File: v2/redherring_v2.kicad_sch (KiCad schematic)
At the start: 182 parts, among them J4 Pimaroni Trackball, Q2 TIP120, SW1 SW_PUSH_LED, SW10 SW_PUSH_LED, SW11 SW_PUSH_LED, SW12 SW_PUSH_LED, SW13 SW_PUSH_LED, SW14 SW_PUSH_LED, SW15 SW_PUSH_LED, SW16 SW_PUSH_LED, SW17 SW_PUSH_LED, SW18 SW_PUSH_LED, SW19 SW_PUSH_LED, SW2 SW_PUSH_LED, SW20 SW_PUSH_LED, SW21 SW_PUSH_LED, SW22 SW_PUSH_LED, SW23 SW_PUSH_LED, SW24 SW_PUSH_LED, SW25 SW_PUSH_LED, SW26 SW_PUSH_LED, SW27 SW_PUSH_LED, SW28 SW_PUSH_LED, SW29 SW_PUSH_LED, SW3 SW_PUSH_LED, SW30 SW_PUSH_LED, SW31 SW_PUSH_LED, SW32 SW_PUSH_LED, SW33 SW_PUSH_LED, SW34 SW_PUSH_LED, SW35 SW_PUSH_LED, SW36 SW_PUSH_LED, SW37 SW_PUSH_LED, SW38 SW_PUSH_LED, SW39 SW_PUSH_LED, SW4 SW_PUSH_LED, SW40 SW_PUSH_LED, SW41 SW_PUSH_LED, SW42 SW_PUSH_LED, SW43 SW_PUSH_LED, SW44 SW_PUSH_LED, SW45 SW_PUSH_LED, SW46 SW_PUSH_LED, SW47 SW_PUSH_LED, SW48 SW_PUSH_LED, SW49 SW_PUSH_LED, SW5 SW_PUSH_LED, SW50 SW_PUSH_LED, SW51 SW_PUSH_LED, SW52 SW_PUSH_LED, SW53 SW_PUSH_LED, SW54 SW_PUSH_LED, SW55 SW_PUSH_LED, SW56 SW_PUSH_LED, SW57 SW_PUSH_LED, SW58 SW_PUSH_LED, SW59 SW_PUSH_LED, SW6 SW_PUSH_LED, SW60 SW_PUSH_LED, SW61 SW_PUSH_LED, SW62 SW_PUSH_LED, SW63 SW_PUSH_LED, SW64 SW_PUSH_LED, SW65 SW_PUSH_LED, SW66 SW_PUSH_LED, SW67 SW_PUSH_LED, SW68 SW_PUSH_LED, SW69 SW_PUSH_LED, SW7 SW_PUSH_LED, SW71 SW_PUSH_LED, SW72 SW_PUSH_LED, SW73 SW_PUSH_LED, SW74 SW_PUSH_LED, SW75 SW_PUSH_LED, SW76 SW_PUSH_LED, SW77 SW_PUSH_LED, SW78 SW_PUSH_LED, SW79 SW_PUSH_LED, SW8 SW_PUSH_LED, SW81 SW_PUSH_LED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

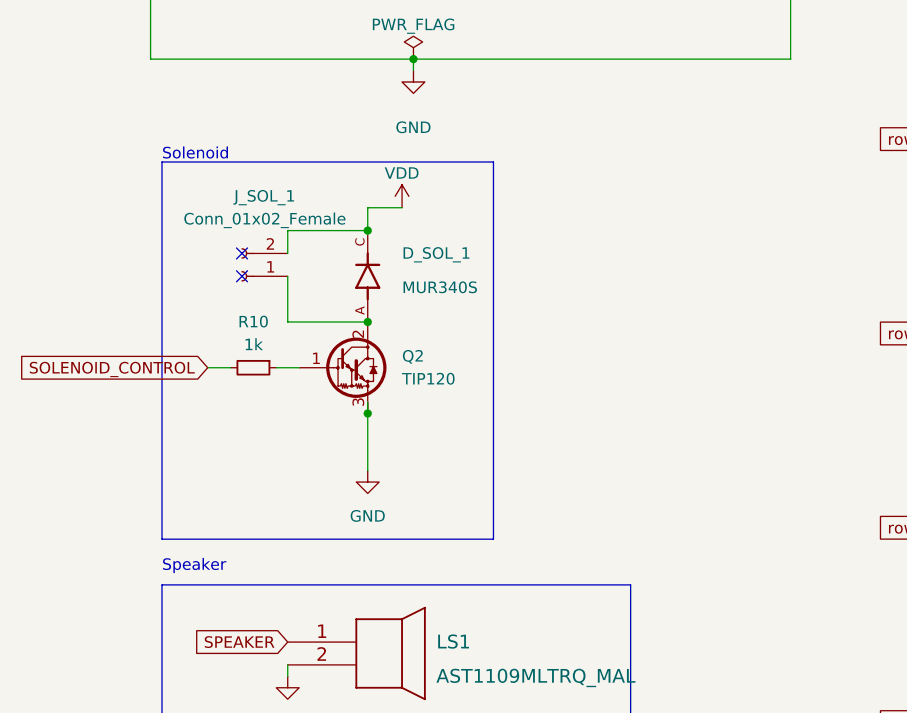
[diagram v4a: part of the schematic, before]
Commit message: Added 3d models
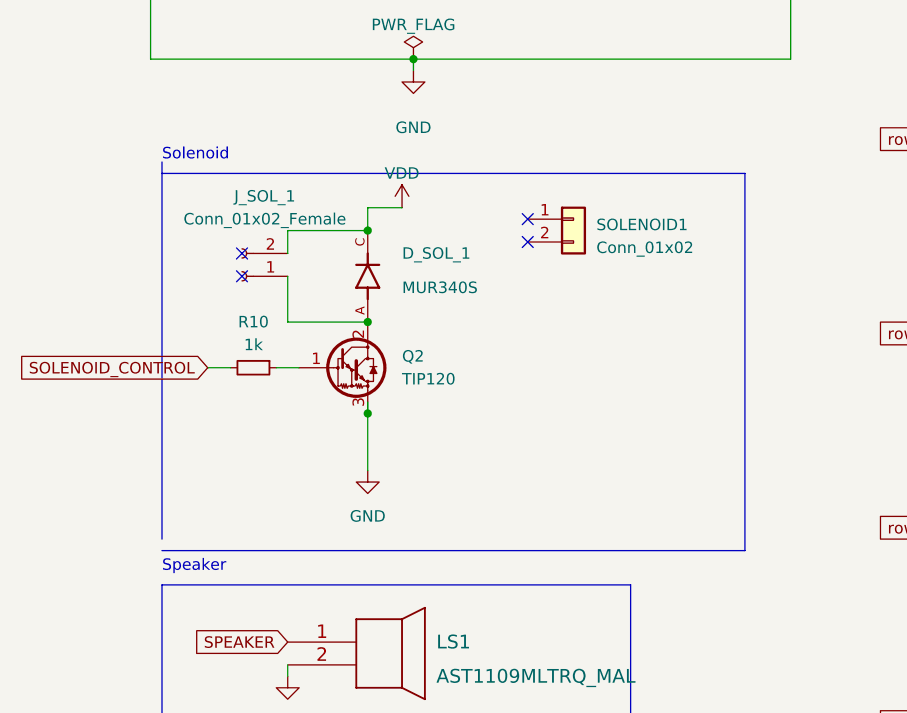
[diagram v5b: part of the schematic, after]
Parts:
- added SOLENOID1: Conn_01x02, red_herring_v2_footprints:uxcell a14092600ux0438 solenoid, symbol Connector_Generic:Conn_01x02
- LS1: footprint ergodonk_kicad_library:AST1109MLTRQ CANTOR MX -> red_herring_v2_footprints:AST1109MLTRQ CANTOR MX
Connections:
- no-connect marks 11 -> 13
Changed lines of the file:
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@@
   (junction (at 248.92 149.86) (diameter 0) (color 0 0 0 0)
   )
+  (no_connect (at 58.42 101.6))
   (no_connect (at 26.67 107.95))
   (no_connect (at 48.26 76.2))
@@
   (no_connect (at 63.5 33.02))
   (no_connect (at 63.5 30.48))
+  (no_connect (at 58.42 104.14))
   (wire (pts (xy 130.81 200.66) (xy 149.86 200.66))
     (stroke (width 0) (type default))
@@
     (stroke (width 0) (type default))
   )
-  (polyline (pts (xy 17.78 95.25) (xy 54.61 95.25))
+  (polyline (pts (xy 17.78 96.52) (xy 82.55 96.52))
     (stroke (width 0) (type default))
   )
@@
     (stroke (width 0) (type default))
   )
-  (polyline (pts (xy 17.78 137.16) (xy 54.61 137.16))
+  (polyline (pts (xy 17.78 138.43) (xy 82.55 138.43))
     (stroke (width 0) (type default))
   )
@@
     (stroke (width 0) (type default))
   )
-  (polyline (pts (xy 54.61 137.16) (xy 54.61 95.25))
+  (polyline (pts (xy 82.55 138.43) (xy 82.55 96.52))
     (stroke (width 0) (type default))
   )
@@
     )
   )
+  (symbol (lib_id "Connector_Generic:Conn_01x02") (at 63.5 101.6 0) (unit 1)
+    (in_bom yes) (on_board yes) (dnp no) (fields_autoplaced)
+    (property "Reference" "SOLENOID1" (at 66.04 102.235 0)
+      (effects (font (size 1.27 1.27)) (justify left))
+    )
+    (property "Value" "Conn_01x02" (at 66.04 104.775 0)
+      (effects (font (size 1.27 1.27)) (justify left))
+    )
+    (property "Footprint" "red_herring_v2_footprints:uxcell a14092600ux0438 solenoid" (at 63.5 101.6 0)
+      (effects (font (size 1.27 1.27)) hide)
+    )
+    (property "Datasheet" "~" (at 63.5 101.6 0)
+      (effects (font (size 1.27 1.27)) hide)
+    )
+    (pin "1")
+    (pin "2")
+    (instances
+      (project "redherring_v2"
+        (path "/ac76b486-7d71-4fdd-84d6-1ecd5326b6c6"
+          (reference "SOLENOID1") (unit 1)
+        )
+      )
+    )
+  )
   (symbol (lib_id "Device:D") (at 130.81 45.72 270) (mirror x) (unit 1)
     (in_bom yes) (on_board yes) (dnp no)
@@
       (effects (font (size 1.524 1.524)) (justify left))
     )
-    (property "Footprint" "ergodonk_kicad_library:AST1109MLTRQ CANTOR MX" (at 39.37 145.034 0)
+    (property "Footprint" "red_herring_v2_footprints:AST1109MLTRQ CANTOR MX" (at 39.37 145.034 0)
       (effects (font (size 1.524 1.524)) hide)
     )

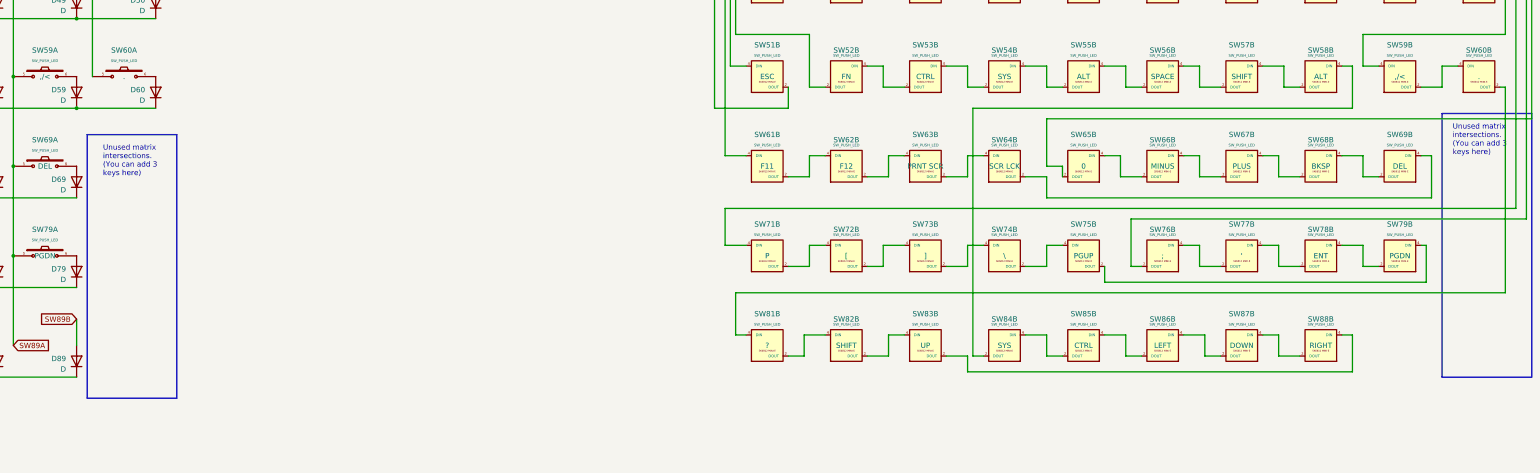
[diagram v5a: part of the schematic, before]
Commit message: Placed two additional keys
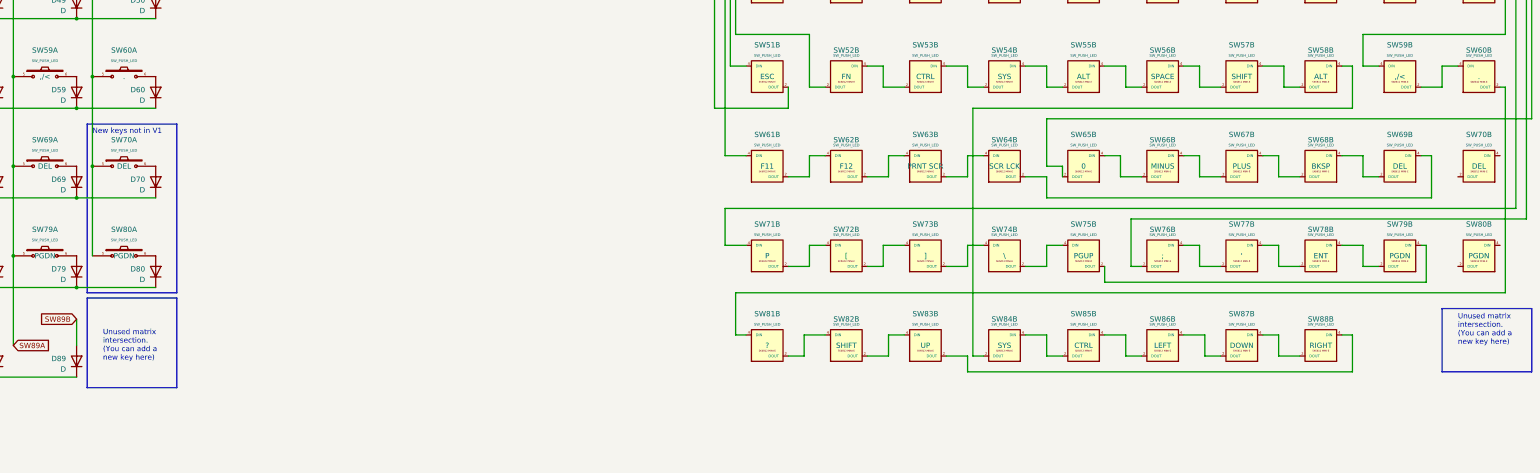
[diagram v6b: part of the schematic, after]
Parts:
- added D70, D80: D, red_herring_v2_footprints:D_SOD-123_DO-35_Hybrid_DoubleSided, symbol Device:D
- added SW70, SW80: SW_PUSH_LED, red_herring_v2_footprints:V2_CherryMX_DS_Hotswap_miniE_1U_SEED_LH, symbol red_herring_v2:SW_PUSH_LED
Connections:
- net GND: now also SW70.3 (GND), SW80.3 (GND)
- net VDD: now also SW70.1 (VDD), SW80.1 (VDD)
- net col10: now also SW70.5, SW80.5
- net row7: now also D70.1 (K)
- net row8: now also D80.1 (K)
- new net: D80.2 (A), SW80.6
- new net: D70.2 (A), SW70.6
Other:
- note added: "New keys not in V1"
- note added: "Unused matrix intersection. (You can add a new key here)"
- note removed: "Unused matrix intersections. (You can add 3 keys here)"

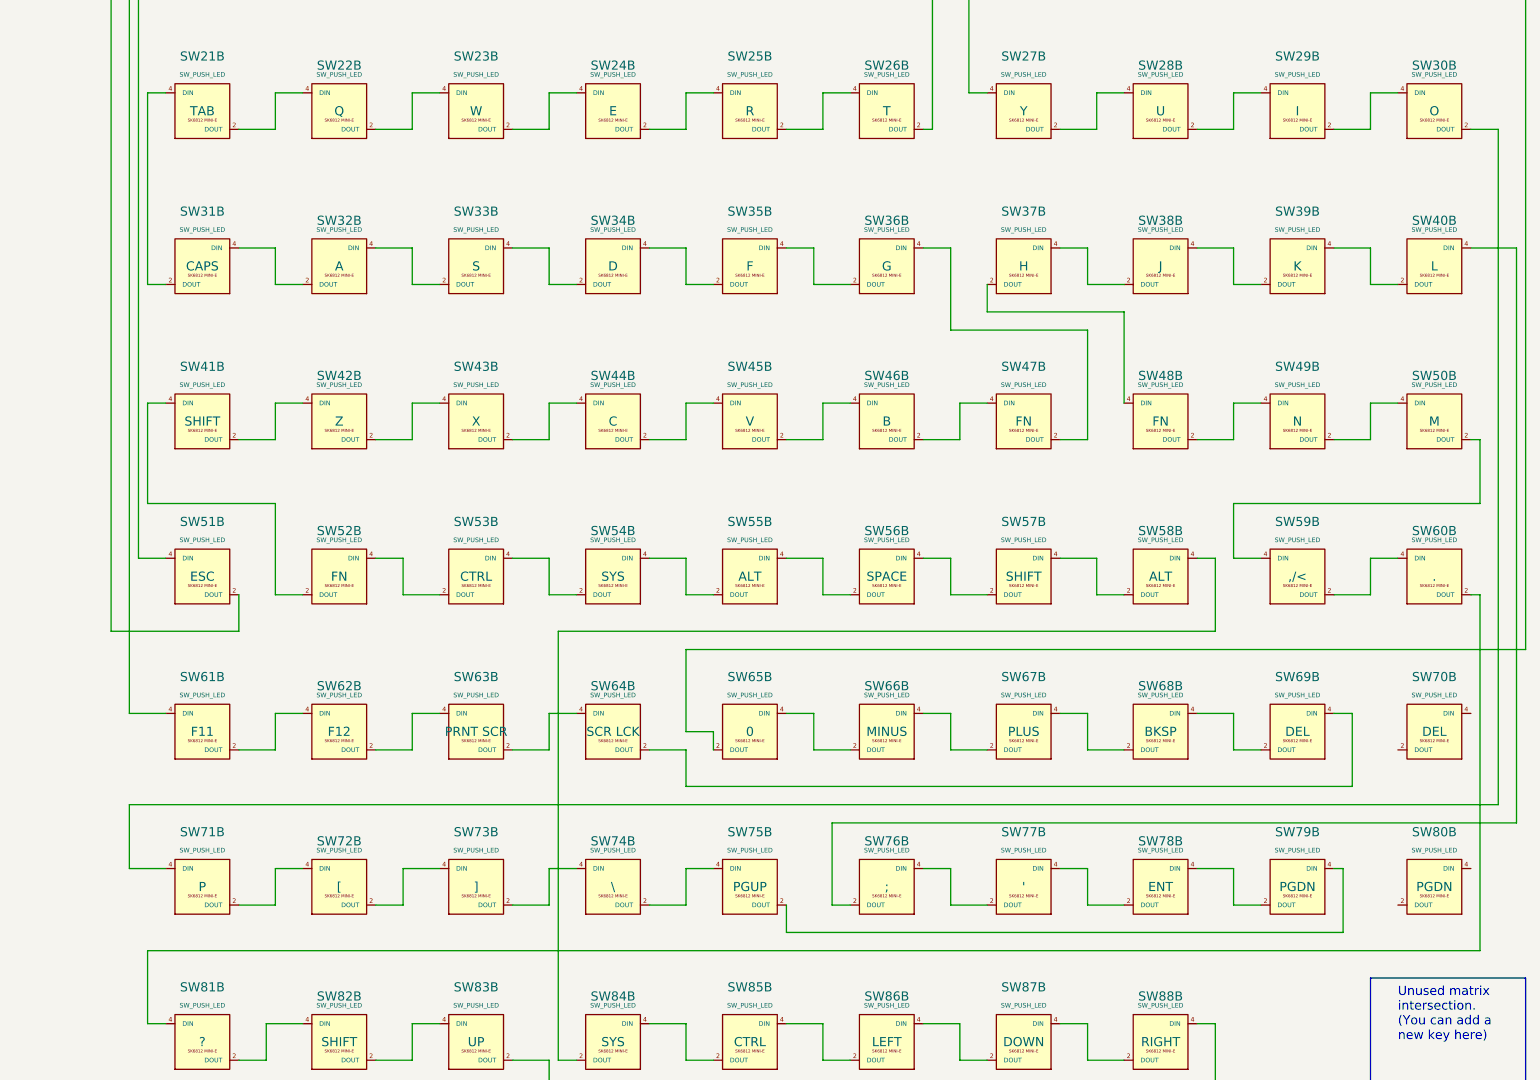
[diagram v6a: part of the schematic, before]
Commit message: Outline reduced to 1.5mm
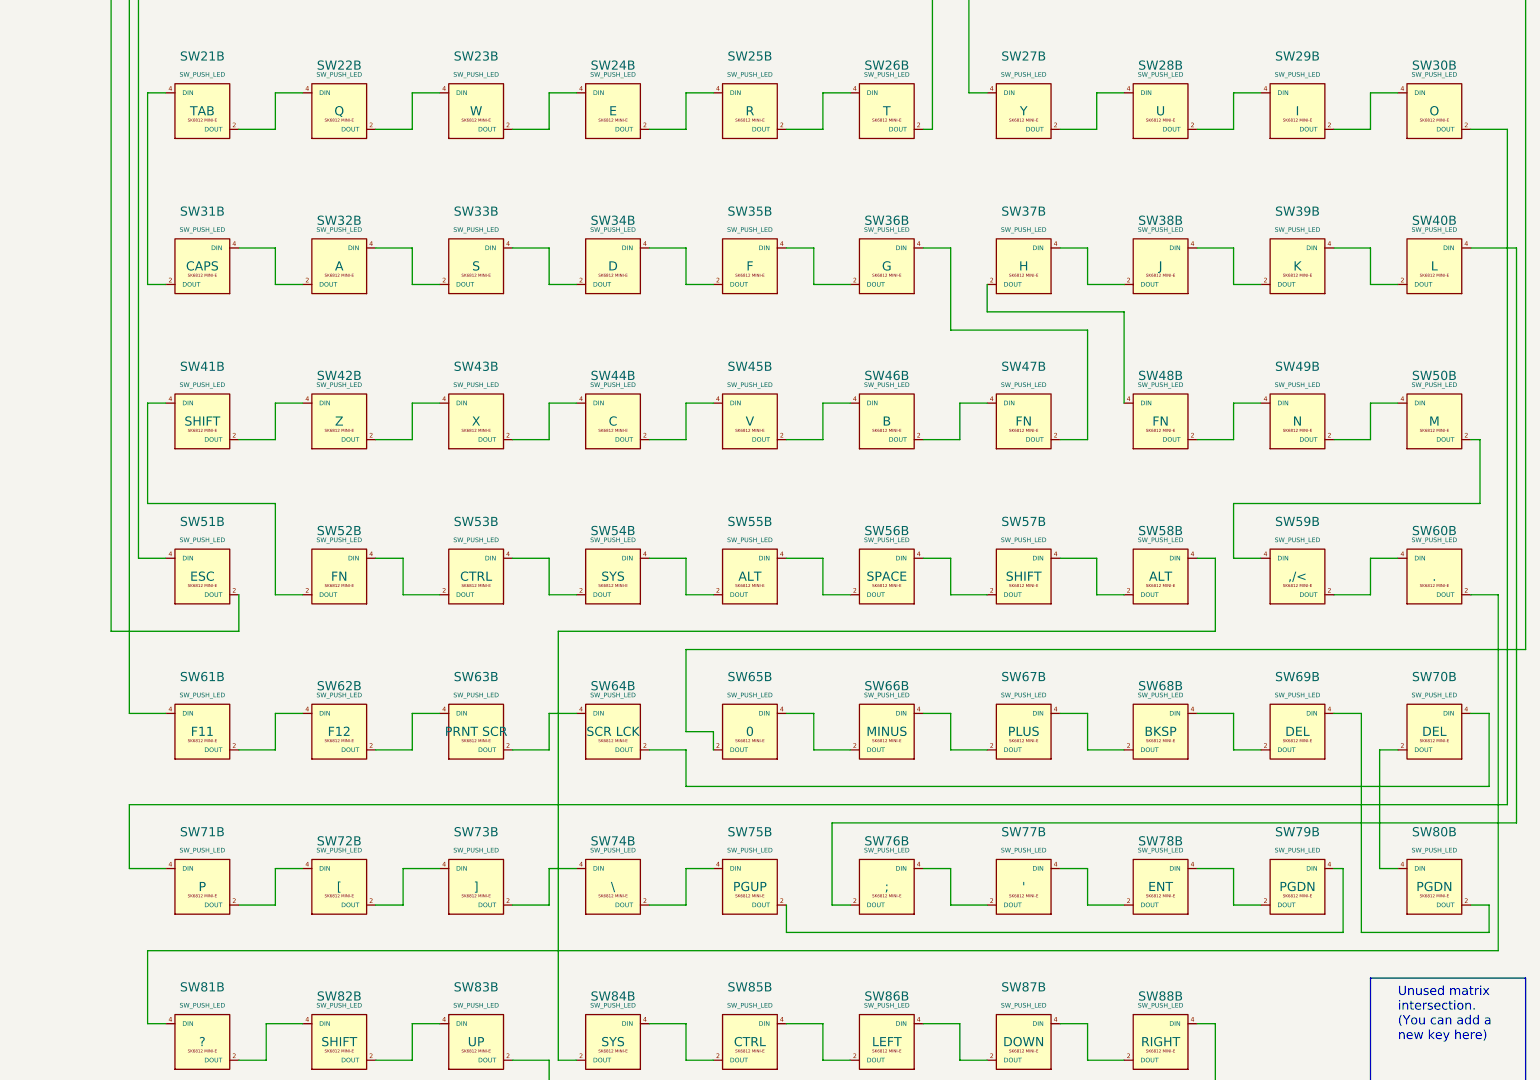
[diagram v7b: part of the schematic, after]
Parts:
- J4: footprint red_herring_v2_footprints:pimoroni_trackball -> red_herring_v2_footprints:pimoroni_trackball_tiein
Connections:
- net at SW70.2 (DOUT): now also SW80.4 (DIN)
- net at SW70.4 (DIN): now also SW64.2 (DOUT)
- net at SW80.2 (DOUT): now also SW69.4 (DIN)
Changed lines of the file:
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@@
     (stroke (width 0) (type default))
   )
-  (wire (pts (xy 627.38 152.4) (xy 627.38 201.93))
+  (wire (pts (xy 629.92 152.4) (xy 629.92 201.93))
     (stroke (width 0) (type default))
   )
-  (wire (pts (xy 627.38 201.93) (xy 441.96 201.93))
+  (wire (pts (xy 629.92 201.93) (xy 441.96 201.93))
     (stroke (width 0) (type default))
   )
@@
     (stroke (width 0) (type default))
   )
+  (wire (pts (xy 628.65 179.07) (xy 628.65 168.91))
+    (stroke (width 0) (type default))
+  )
   (wire (pts (xy 607.06 190.5) (xy 608.33 190.5))
     (stroke (width 0) (type default))
@@
     (stroke (width 0) (type default))
   )
+  (wire (pts (xy 628.65 195.58) (xy 628.65 199.39))
+    (stroke (width 0) (type default))
+  )
   (wire (pts (xy 497.84 195.58) (xy 497.84 190.5))
     (stroke (width 0) (type default))
@@
     (stroke (width 0) (type default))
   )
-  (wire (pts (xy 609.6 179.07) (xy 609.6 168.91))
-    (stroke (width 0) (type default))
-  )
   (wire (pts (xy 229.87 128.27) (xy 229.87 149.86))
     (stroke (width 0) (type default))
@@
     (stroke (width 0) (type default))
   )
-  (wire (pts (xy 629.92 181.61) (xy 439.42 181.61))
+  (wire (pts (xy 631.19 181.61) (xy 439.42 181.61))
     (stroke (width 0) (type default))
   )
@@
     (stroke (width 0) (type default))
   )
+  (wire (pts (xy 628.65 168.91) (xy 626.11 168.91))
+    (stroke (width 0) (type default))
+  )
   (wire (pts (xy 287.02 106.68) (xy 287.02 128.27))
     (stroke (width 0) (type default))
@@
     (stroke (width 0) (type default))
   )
+  (wire (pts (xy 615.95 173.99) (xy 613.41 173.99))
+    (stroke (width 0) (type default))
+  )
   (wire (pts (xy 134.62 85.09) (xy 134.62 106.68))
     (stroke (width 0) (type default))
   )
+  (wire (pts (xy 628.65 199.39) (xy 610.87 199.39))
+    (stroke (width 0) (type default))
+  )
   (wire (pts (xy 632.46 184.15) (xy 632.46 104.14))
     (stroke (width 0) (type default))
@@
     (stroke (width 0) (type default))
   )
-  (wire (pts (xy 626.11 87.63) (xy 629.92 87.63))
+  (wire (pts (xy 626.11 87.63) (xy 631.19 87.63))
     (stroke (width 0) (type default))
   )
@@
     (stroke (width 0) (type default))
   )
+  (wire (pts (xy 610.87 199.39) (xy 610.87 168.91))
+    (stroke (width 0) (type default))
+  )
   (wire (pts (xy 440.69 147.32) (xy 444.5 147.32))
     (stroke (width 0) (type default))
@@
     (stroke (width 0) (type default))
   )
+  (wire (pts (xy 626.11 195.58) (xy 628.65 195.58))
+    (stroke (width 0) (type default))
+  )
   (wire (pts (xy 539.75 66.04) (xy 535.94 66.04))
     (stroke (width 0) (type default))
@@
     (stroke (width 0) (type default))
   )
-  (wire (pts (xy 609.6 168.91) (xy 607.06 168.91))
-    (stroke (width 0) (type default))
-  )
   (wire (pts (xy 207.01 92.71) (xy 226.06 92.71))
     (stroke (width 0) (type default))
@@
     (stroke (width 0) (type default))
   )
+  (wire (pts (xy 610.87 168.91) (xy 607.06 168.91))
+    (stroke (width 0) (type default))
+  )
   (wire (pts (xy 16.51 53.34) (xy 27.94 53.34))
     (stroke (width 0) (type default))
@@
     (stroke (width 0) (type default))
   )
-  (wire (pts (xy 516.89 179.07) (xy 609.6 179.07))
+  (wire (pts (xy 516.89 179.07) (xy 628.65 179.07))
     (stroke (width 0) (type default))
   )
@@
     (stroke (width 0) (type default))
   )
+  (wire (pts (xy 613.41 190.5) (xy 615.95 190.5))
+    (stroke (width 0) (type default))
+  )
   (wire (pts (xy 264.16 49.53) (xy 283.21 49.53))
     (stroke (width 0) (type default))
@@
     (stroke (width 0) (type default))
   )
-  (wire (pts (xy 629.92 87.63) (xy 629.92 181.61))
+  (wire (pts (xy 631.19 87.63) (xy 631.19 181.61))
     (stroke (width 0) (type default))
   )
@@
     (stroke (width 0) (type default))
   )
-  (wire (pts (xy 626.11 152.4) (xy 627.38 152.4))
+  (wire (pts (xy 626.11 152.4) (xy 629.92 152.4))
     (stroke (width 0) (type default))
   )
@@
     (stroke (width 0) (type default))
   )
+  (wire (pts (xy 613.41 173.99) (xy 613.41 190.5))
+    (stroke (width 0) (type default))
+  )
   (wire (pts (xy 45.72 85.09) (xy 45.72 83.82))
     (stroke (width 0) (type default))
@@
     )
   )
-  (symbol (lib_id "red_herring_v2:SW_PUSH_LED") (at 621.03 193.04 0) (unit 2)
-    (in_bom yes) (on_board yes) (dnp no) (fields_autoplaced)
+  (symbol (lib_id "red_herring_v2:SW_PUSH_LED") (at 621.03 193.04 0) (mirror y) (unit 2)
+    (in_bom yes) (on_board yes) (dnp no)
     (property "Reference" "SW80" (at 621.03 185.42 0)
       (effects (font (size 1.27 1.27)))
@@
       (effects (font (size 0.635 0.635)))
     )
-    (property "Footprint" "red_herring_v2_footprints:V2_CherryMX_DS_Hotswap_miniE_1U_SEED_LH" (at 621.792 187.96 0)
+    (property "Footprint" "red_herring_v2_footprints:V2_CherryMX_DS_Hotswap_miniE_1U_SEED_LH" (at 620.268 187.96 0)
       (effects (font (size 1.27 1.27)) hide)
     )
@@
       (effects (font (size 1.27 1.27)) (justify left) hide)
     )
-    (property "Footprint" "red_herring_v2_footprints:pimoroni_trackball" (at 31.75 240.03 0)
+    (property "Footprint" "red_herring_v2_footprints:pimoroni_trackball_tiein" (at 31.75 240.03 0)
       (effects (font (size 1.27 1.27)) hide)
     )
